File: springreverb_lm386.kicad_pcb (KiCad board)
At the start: 2 copper layers, 69.9 x 55.3 mm, 54 parts, among them J1 IN, J10 VR2_3, J11 VR_2_2, J12 VR_2GND, J13 To, J14 FromSW, J17 FromGND, J18 From, J19 VR3_3, J2 INGND, J20 VR_4_3, J21 VR4_1, J3 GND, J4 Vin, J5 LEDGND, J6 VR1_3, J7 toC6, J8 toC7, J9 FromC, U1 TL072, U2 TC1044S, U3 LM386

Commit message: 接続の名称を変更
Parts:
- J9: value FromC -> FromC1

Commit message: 不要な配線を修正
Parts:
- removed J12: VR_2GND, MyLibrary:PinHeader_1x01_P2.54mm_Vertical
- J9: value FromC1 -> VR_1_1

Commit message: LM386に向かうCの値を変更
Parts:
- C6: value 0.1u -> 0.047u
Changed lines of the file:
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@@
 			)
 		)
-		(property "Value" "0.1u"
+		(property "Value" "0.047u"
 			(at 0.05 0.9 90)
 			(unlocked yes)
@@
 		(layer "F.Cu")
 		(hatch none 0.1)
-		(priority 30000)
+		(priority 30001)
 		(attr
 			(teardrop
@@
 		(polygon
 			(pts
-				(xy 71.64 108.268609) (xy 73.14 108.268609) (xy 73.39 106.624877) (xy 72.39 106.167609) (xy 71.39 106.624877)
+				(xy 73.14 111.692) (xy 71.64 111.692) (xy 71.400648 112.923619) (xy 72.39 113.793) (xy 73.379352 112.923619)
 			)
 		)
@@
 		(layer "F.Cu")
 		(hatch none 0.1)
-		(priority 30001)
+		(priority 30000)
 		(attr
 			(teardrop
@@
 		(polygon
 			(pts
-				(xy 73.14 111.692) (xy 71.64 111.692) (xy 71.400648 112.923619) (xy 72.39 113.793) (xy 73.379352 112.923619)
+				(xy 71.64 108.268609) (xy 73.14 108.268609) (xy 73.39 106.624877) (xy 72.39 106.167609) (xy 71.39 106.624877)
 			)
 		)
 	)
 	(zone
-		(net "Net-(J16-In)")
+		(net "Net-(C3-Pad1)")
 		(layer "B.Cu")
 		(hatch none 0.1)
-		(priority 30016)
+		(priority 30006)
 		(attr
 			(teardrop
@@
 		(polygon
 			(pts
-				(xy 95.5404 89.1376) (xy 93.7404 89.1376) (xy 93.6404 90.1376) (xy 94.6404 91.2886) (xy 95.6404 90.1376)
+				(xy 68.464 101.179791) (xy 66.664 101.179791) (xy 66.564 102.823522) (xy 67.564 103.280791) (xy 68.564 102.823522)
 			)
 		)
@@
 		(layer "B.Cu")
 		(hatch none 0.1)
-		(priority 30001)
+		(priority 30013)
 		(attr
 			(teardrop
@@
 		(polygon
 			(pts
-				(xy 66.7148 105.373009) (xy 68.5148 105.373009) (xy 68.6148 103.591071) (xy 67.6148 103.272009)
-				(xy 66.6148 103.828978)
+				(xy 92.541425 94.433999) (xy 92.541425 96.233999) (xy 93.082401 96.233999) (xy 93.718797 95.970395)
+				(xy 94.569274 95.261339) (xy 94.185505 94.230895) (xy 93.15506 93.847125) (xy 92.446005 94.697603)
+				(xy 93.082401 94.433999)
 			)
 		)
 	)
 	(zone
-		(net "Net-(C12-Pad2)")
+		(net "GND")
 		(layer "B.Cu")
 		(hatch none 0.1)
-		(priority 30010)
+		(priority 30015)
 		(attr
 			(teardrop
@@
 		(polygon
 			(pts
-				(xy 92.13453 100.213722) (xy 93.407322 98.94093) (xy 92.315739 97.707926) (xy 91.285295 98.091695)
-				(xy 90.901526 99.122139)
+				(xy 90.0062 90.7436) (xy 91.8062 90.7436) (xy 91.9062 89.7436) (xy 90.9062 88.4926) (xy 89.9062 89.7436)
 			)
 		)
 	)
 	(zone
-		(net "Net-(U1C-V+)")
+		(net "Net-(J16-In)")
 		(layer "B.Cu")
 		(hatch none 0.1)
-		(priority 30000)
+		(priority 30016)
 		(attr
 			(teardrop
@@
 		(polygon
 			(pts
-				(xy 104.35113 90.002922) (xy 105.623922 88.73013) (xy 104.532339 87.497126) (xy 103.501895 87.880895)
-				(xy 103.118126 88.911339)
+				(xy 95.5404 89.1376) (xy 93.7404 89.1376) (xy 93.6404 90.1376) (xy 94.6404 91.2886) (xy 95.6404 90.1376)
 			)
 		)
 	)
 	(zone
-		(net "Net-(C12-Pad2)")
+		(net "GND")
 		(layer "B.Cu")
 		(hatch none 0.1)
-		(priority 30005)
+		(priority 30003)
 		(attr
 			(teardrop
@@
 		(polygon
 			(pts
-				(xy 89.191791 97.1948) (xy 89.191791 98.9948) (xy 90.835522 99.0948) (xy 91.292791 98.0948) (xy 90.835522 97.0948)
+				(xy 92.050391 76.189) (xy 92.050391 77.989) (xy 93.694122 78.089) (xy 94.151391 77.089) (xy 93.694122 76.089)
 			)
 		)
@@
 		(layer "B.Cu")
 		(hatch none 0.1)
-		(priority 30011)
+		(priority 30007)
 		(attr
 			(teardrop
@@
 		(polygon
 			(pts
-				(xy 66.71787 101.157478) (xy 65.445078 102.43027) (xy 66.53666 103.663273) (xy 67.567105 103.279505)
-				(xy 67.950873 102.24906)
+				(xy 68.5148 103.549091) (xy 66.7148 103.549091) (xy 66.6148 105.192822) (xy 67.6148 105.650091)
+				(xy 68.6148 105.192822)
 			)
 		)
 	)
 	(zone
-		(net "Net-(U1C-V+)")
+		(net "Net-(C3-Pad1)")
 		(layer "B.Cu")
 		(hatch none 0.1)
-		(priority 30001)
+		(priority 30011)
 		(attr
 			(teardrop
@@
 		(polygon
 			(pts
-				(xy 105.540747 89.145) (xy 105.540747 87.345) (xy 104.396223 87.245) (xy 103.439747 88.245) (xy 103.439747 88.980609)
+				(xy 66.71787 101.157478) (xy 65.445078 102.43027) (xy 66.53666 103.663273) (xy 67.567105 103.279505)
+				(xy 67.950873 102.24906)
 			)
 		)
@@
 		(layer "B.Cu")
 		(hatch none 0.1)
-		(priority 30009)
+		(priority 30010)
 		(attr
 			(teardrop
@@
 		(polygon
 			(pts
-				(xy 86.24093 97.724522) (xy 87.513722 96.45173) (xy 86.422139 95.218726) (xy 85.391695 95.602495)
-				(xy 85.007926 96.632939)
+				(xy 92.13453 100.213722) (xy 93.407322 98.94093) (xy 92.315739 97.707926) (xy 91.285295 98.091695)
+				(xy 90.901526 99.122139)
 			)
 		)
@@
 	)
 	(zone
-		(net "Net-(C3-Pad1)")
+		(net "Net-(J1-Pin_1)")
 		(layer "B.Cu")
 		(hatch none 0.1)
-		(priority 30006)
+		(priority 30017)
 		(attr
 			(teardrop
@@
 		(polygon
 			(pts
-				(xy 68.464 101.179791) (xy 66.664 101.179791) (xy 66.564 102.823522) (xy 67.564 103.280791) (xy 68.564 102.823522)
+				(xy 117.232 93.609) (xy 115.432 93.609) (xy 115.332 94.609) (xy 116.332 95.76) (xy 117.332 94.609)
 			)
 		)
 	)
 	(zone
-		(net "GND")
+		(net "Net-(C12-Pad2)")
 		(layer "B.Cu")
 		(hatch none 0.1)
-		(priority 30003)
+		(priority 30009)
 		(attr
 			(teardrop
@@
 		(polygon
 			(pts
-				(xy 92.050391 76.189) (xy 92.050391 77.989) (xy 93.694122 78.089) (xy 94.151391 77.089) (xy 93.694122 76.089)
+				(xy 86.24093 97.724522) (xy 87.513722 96.45173) (xy 86.422139 95.218726) (xy 85.391695 95.602495)
+				(xy 85.007926 96.632939)
 			)
 		)
 	)
 	(zone
-		(net "Net-(U1C-V-)")
+		(net "GND")
 		(layer "B.Cu")
 		(hatch none 0.1)
@@
 		(polygon
 			(pts
-				(xy 97.547 78.44473) (xy 95.747 78.44473) (xy 95.747 78.503213) (xy 96.010604 77.866817) (xy 94.947096 79.689252)
-				(xy 95.202722 79.947491) (xy 96.840547 79.723879) (xy 97.283396 79.139609) (xy 97.547 78.503213)
+				(xy 83.8256 115.073591) (xy 82.0256 115.073591) (xy 81.9256 116.717322) (xy 82.9256 117.174591)
+				(xy 83.9256 116.717322)
 			)
 		)
@@
 		(layer "B.Cu")
 		(hatch none 0.1)
-		(priority 30004)
+		(priority 30002)
 		(attr
 			(teardrop
@@
 		(polygon
 			(pts
-				(xy 86.2948 85.888991) (xy 84.4948 85.888991) (xy 84.3948 87.532722) (xy 85.3948 87.989991) (xy 86.3948 87.532722)
+				(xy 97.547 78.44473) (xy 95.747 78.44473) (xy 95.747 78.503213) (xy 96.010604 77.866817) (xy 94.947096 79.689252)
+				(xy 95.202722 79.947491) (xy 96.840547 79.723879) (xy 97.283396 79.139609) (xy 97.547 78.503213)
 			)
 		)
 	)
 	(zone
-		(net "Net-(C3-Pad1)")
+		(net "Net-(U1C-V+)")
 		(layer "B.Cu")
 		(hatch none 0.1)
-		(priority 30013)
+		(priority 30000)
 		(attr
 			(teardrop
@@
 		(polygon
 			(pts
-				(xy 92.541425 94.433999) (xy 92.541425 96.233999) (xy 93.082401 96.233999) (xy 93.718797 95.970395)
-				(xy 94.569274 95.261339) (xy 94.185505 94.230895) (xy 93.15506 93.847125) (xy 92.446005 94.697603)
-				(xy 93.082401 94.433999)
+				(xy 104.35113 90.002922) (xy 105.623922 88.73013) (xy 104.532339 87.497126) (xy 103.501895 87.880895)
+				(xy 103.118126 88.911339)
 			)
 		)
 	)
 	(zone
-		(net "Net-(C3-Pad1)")
+		(net "Net-(C12-Pad2)")
 		(layer "B.Cu")
 		(hatch none 0.1)
-		(priority 30007)
+		(priority 30005)
 		(attr
 			(teardrop
@@
 		(polygon
 			(pts
-				(xy 68.5148 103.549091) (xy 66.7148 103.549091) (xy 66.6148 105.192822) (xy 67.6148 105.650091)
-				(xy 68.6148 105.192822)
+				(xy 89.191791 97.1948) (xy 89.191791 98.9948) (xy 90.835522 99.0948) (xy 91.292791 98.0948) (xy 90.835522 97.0948)
 			)
 		)
 	)
 	(zone
-		(net "GND")
+		(net "Net-(U1C-V+)")
 		(layer "B.Cu")
 		(hatch none 0.1)
-		(priority 30002)
+		(priority 30001)
 		(attr
 			(teardrop
@@
 		(polygon
 			(pts
-				(xy 83.8256 115.073591) (xy 82.0256 115.073591) (xy 81.9256 116.717322) (xy 82.9256 117.174591)
-				(xy 83.9256 116.717322)
+				(xy 105.540747 89.145) (xy 105.540747 87.345) (xy 104.396223 87.245) (xy 103.439747 88.245) (xy 103.439747 88.980609)
 			)
 		)
 	)
 	(zone
-		(net "Net-(J1-Pin_1)")
+		(net "Net-(C3-Pad1)")
 		(layer "B.Cu")
 		(hatch none 0.1)
-		(priority 30017)
+		(priority 30001)
 		(attr
 			(teardrop
@@
 		(polygon
 			(pts
-				(xy 117.232 93.609) (xy 115.432 93.609) (xy 115.332 94.609) (xy 116.332 95.76) (xy 117.332 94.609)
+				(xy 66.7148 105.373009) (xy 68.5148 105.373009) (xy 68.6148 103.591071) (xy 67.6148 103.272009)
+				(xy 66.6148 103.828978)
 			)
 		)
 	)
 	(zone
-		(net "GND")
+		(net "Net-(U1C-V-)")
 		(layer "B.Cu")
 		(hatch none 0.1)
-		(priority 30015)
+		(priority 30004)
 		(attr
 			(teardrop
@@
 		(polygon
 			(pts
-				(xy 90.0062 90.7436) (xy 91.8062 90.7436) (xy 91.9062 89.7436) (xy 90.9062 88.4926) (xy 89.9062 89.7436)
+				(xy 86.2948 85.888991) (xy 84.4948 85.888991) (xy 84.3948 87.532722) (xy 85.3948 87.989991) (xy 86.3948 87.532722)
 			)
 		)

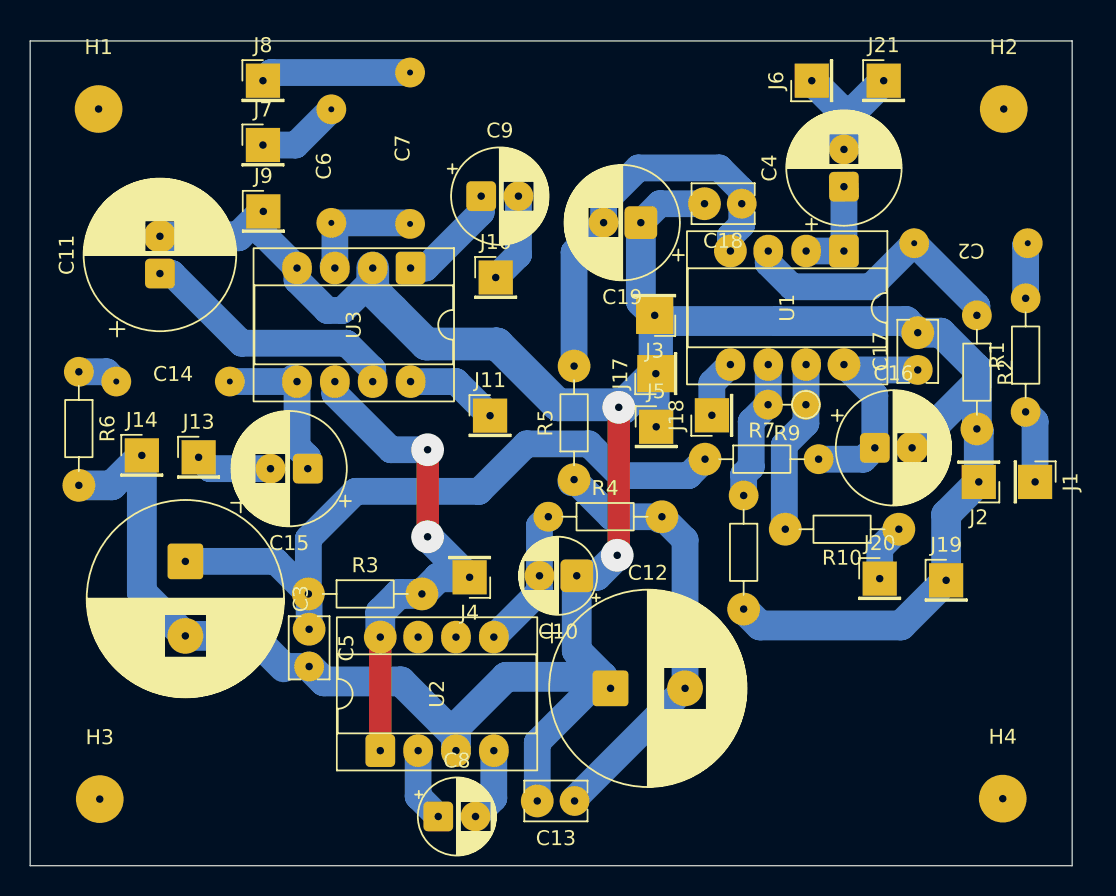
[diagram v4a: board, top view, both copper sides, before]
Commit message: dryをできるだけ原音のままにするため3番ピンから取り出し。 トーンVRで無音になる問題を修正。
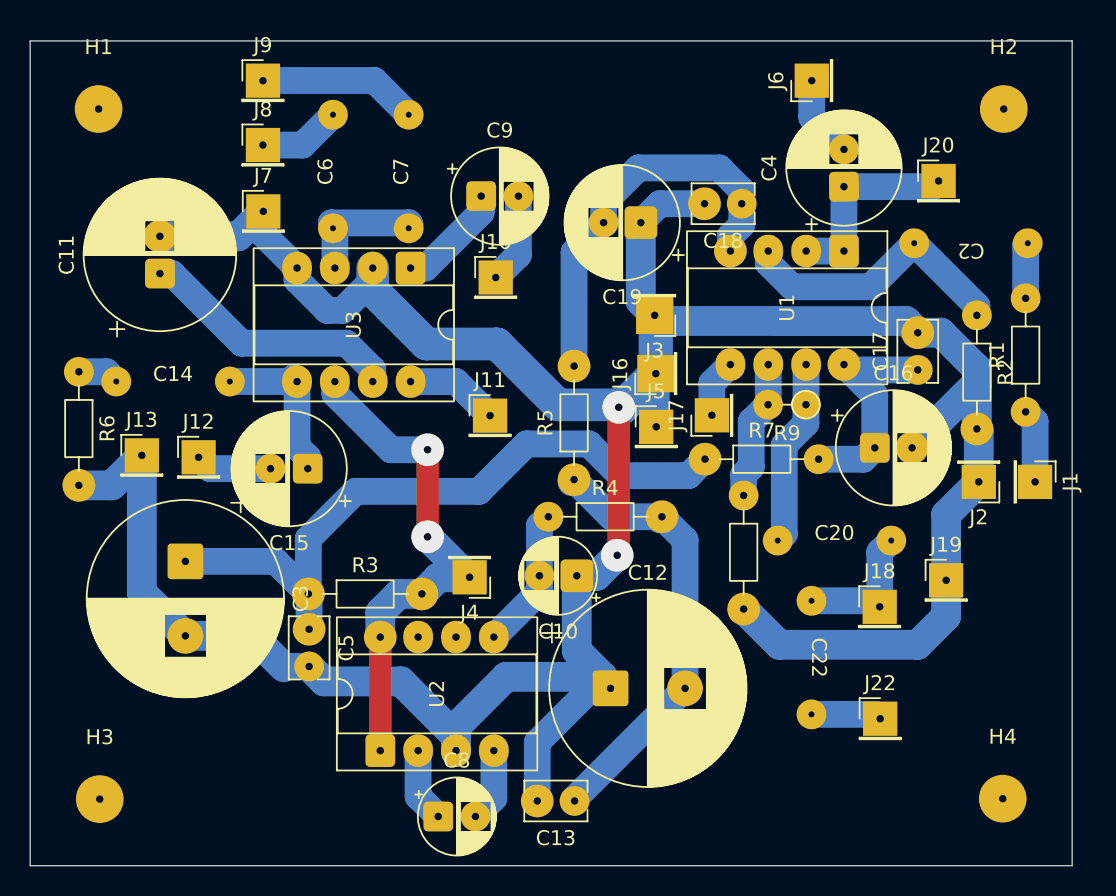
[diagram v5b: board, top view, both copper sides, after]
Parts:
- removed R10: 1k, Resistor_THT:R_Axial_DIN0204_L3.6mm_D1.6mm_P7.62mm_Horizontal
- added C20: 4700p, MyLibrary:9.3_4.3_p7.5, F.Cu at (102.9, 99.7)
- added C22: 0.022u, MyLibrary:9.3_4.3_p7.5, F.Cu at (101.3, 107.5)
- added J22: VR_4_1, MyLibrary:PinHeader_1x01_P2.54mm_Vertical, F.Cu at (105.9, 111.7)
- C6: value 0.047u -> 0.022u
- C7: value 0.22u -> 0.01u; footprint MyLibrary:11.2_4.3_p10 -> MyLibrary:9.3_4.3_p7.5
- J18: renamed from J20; value VR_4_3 -> VR_3_3
- moved J20 7.67 mm to (109.9, 75.6)
- moved J18 1.89 mm to (105.9, 104.1)
- moved C7 1.57 mm to (74.3, 74.9)
- moved C6 0.38 mm to (69.2, 74.9)
- renumbered J13 to J12, J14 to J13, J17 to J16, J18 to J17, J21 to J20, J9 to J7, J7 to J8, J8 to J9
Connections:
- C4 pad 1: Net-(U1A--) -> Net-(J20-Pin_1)
- C4 pad 2: Net-(J21-Pin_1) -> Net-(J6-Pin_1)
- J20 pad 1: Net-(J21-Pin_1) -> Net-(J20-Pin_1)
- J6 pad 1: Net-(J21-Pin_1) -> Net-(J6-Pin_1)
- U1 pad 1: Net-(U1A--) -> Net-(J20-Pin_1)
- U1 pad 2: Net-(U1A--) -> Net-(J20-Pin_1)
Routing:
- net Net-(J20-Pin_1): track 0.00 -> 13.4 mm
- net Net-(J21-Pin_1): track 8.77 -> 0.00 mm
- net Net-(U1A--): track 6.86 -> 0.00 mm
- net Net-(J18-Pin_1): track 3.85 -> 9.51 mm
- net Net-(J6-Pin_1): track 0.00 -> 5.51 mm
- net Net-(J22-Pin_1): track 0.00 -> 4.73 mm
- net GND: track 209.2 -> 211.7 mm
- net Net-(C20-Pad1): track 11.7 -> 12.6 mm
- net Net-(J9-Pin_1): track 10.1 -> 10.7 mm

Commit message: トーン回路周りを修正
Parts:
- removed C22: 0.022u, MyLibrary:9.3_4.3_p7.5
- removed J22: VR_4_1, MyLibrary:PinHeader_1x01_P2.54mm_Vertical
- C20: value 4700p -> 0.022uF
- J18: value VR_3_3 -> VR_4_1
- J19: value VR3_3 -> VR4_3
- J20: value VR4_1 -> VR3_1
- moved C20 2.29 mm to (101.6, 101.6), turned to -90 degrees
- moved J18 1.28 mm to (106.0, 105.4)
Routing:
- net Net-(J18-Pin_1): track 9.51 -> 4.45 mm
- net Net-(J22-Pin_1): track 4.73 -> 0.00 mm
- net GND: track 211.7 -> 208.3 mm
- net Net-(C20-Pad1): track 12.6 -> 11.4 mm
